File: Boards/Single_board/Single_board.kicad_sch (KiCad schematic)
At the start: 9 parts, among them J1 AUX_I2C_1, J2 AUX_I2C_2, J4 ICSP, Q1 SI2306

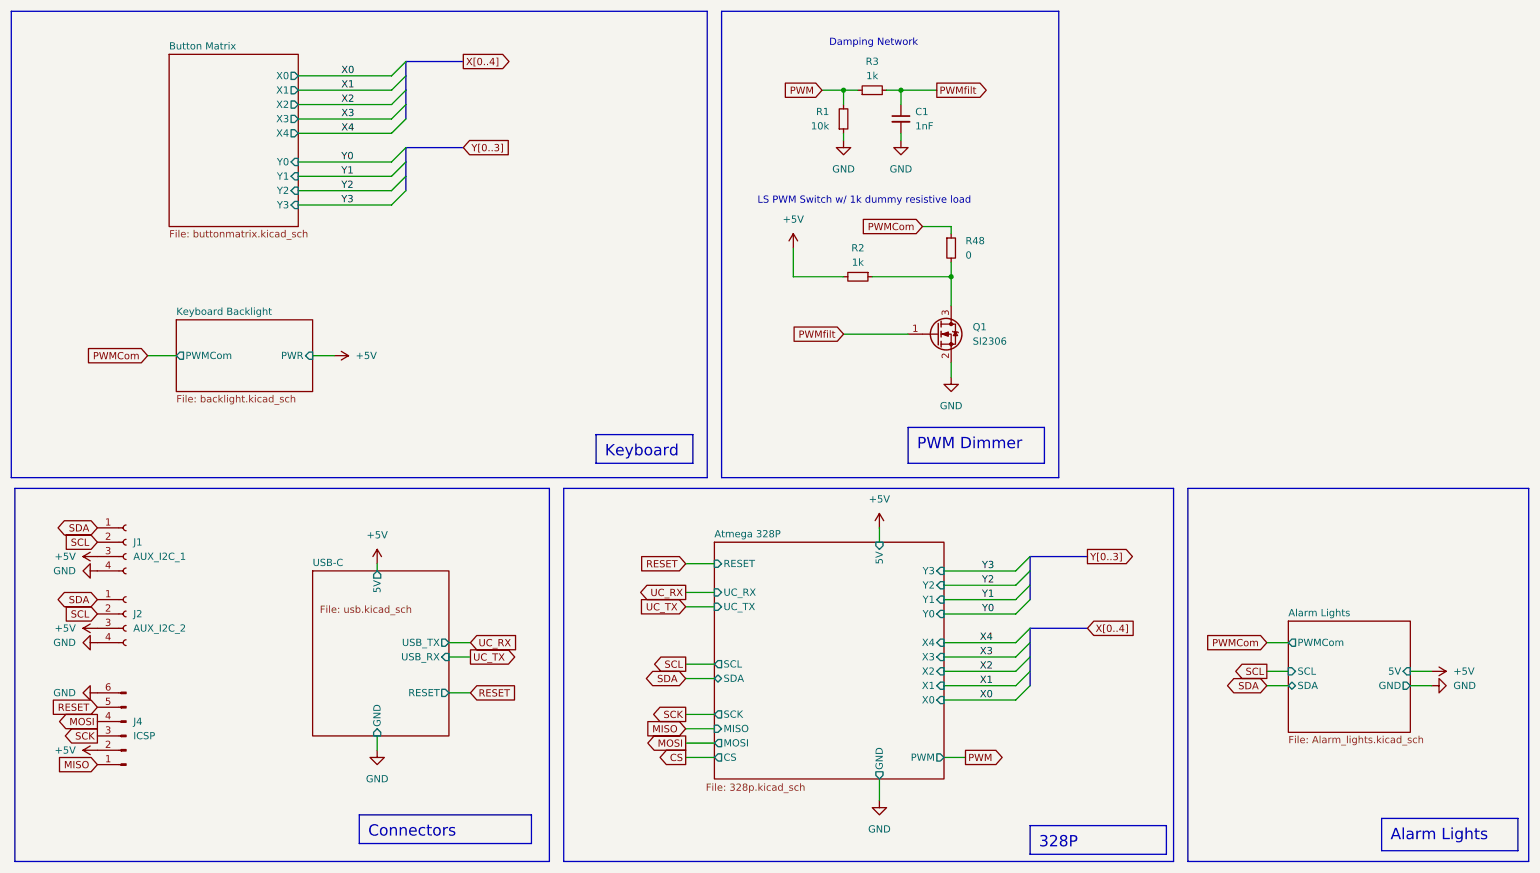
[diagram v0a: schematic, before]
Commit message: Re-stitch and clean up redundant tracks.  Correct some port directions.
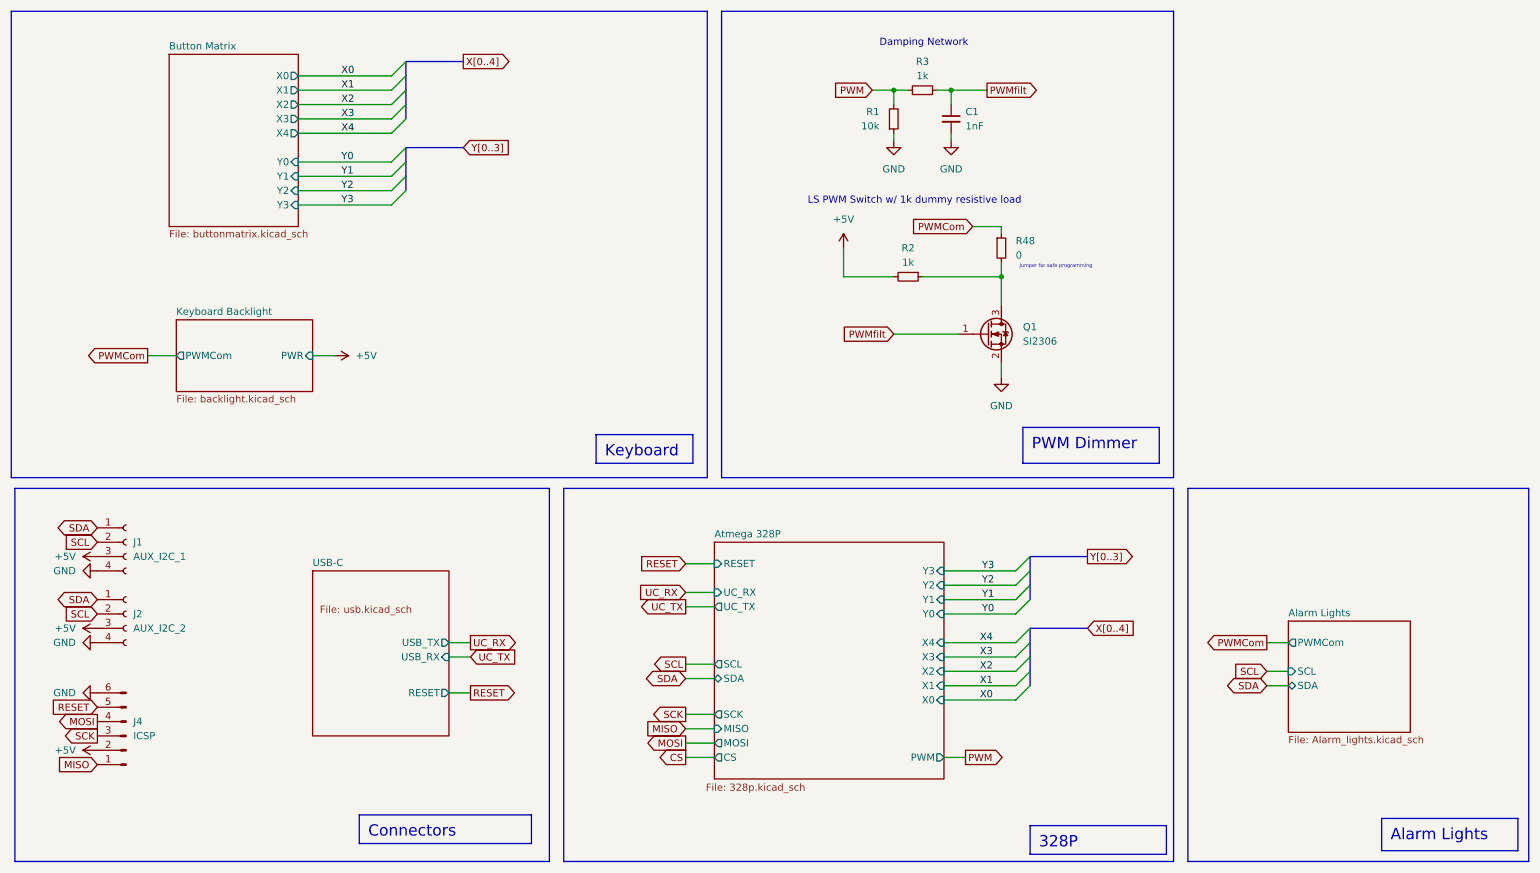
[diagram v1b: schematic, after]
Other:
- sheet Alarm Lights ports: added none; removed 5V, GND
- sheet Atmega 328P ports: added none; removed 5V, GND
- sheet USB-C ports: added none; removed 5V, GND
- note added: "Jumper for safe programming"
- moved on the sheet: C1, Q1, R1, R2, R3, R48

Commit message: Remove redundant GND tracks in place of vias.  Continue rerouting & condensing.  Make PWMCom 20mil
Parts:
- renumbered R48 to SB1
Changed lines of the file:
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@@
 		(dnp no)
 		(fields_autoplaced yes)
-		(property "Reference" "R48"
+		(property "Reference" "SB1"
 			(at 191.77 54.6099 0)
 			(effects
@@
 			(project "Single_board"
 				(path "/f30854c1-5bc2-470d-aabe-1768a5b01b46"
-					(reference "R48")
+					(reference "SB1")
 					(unit 1)
 				)

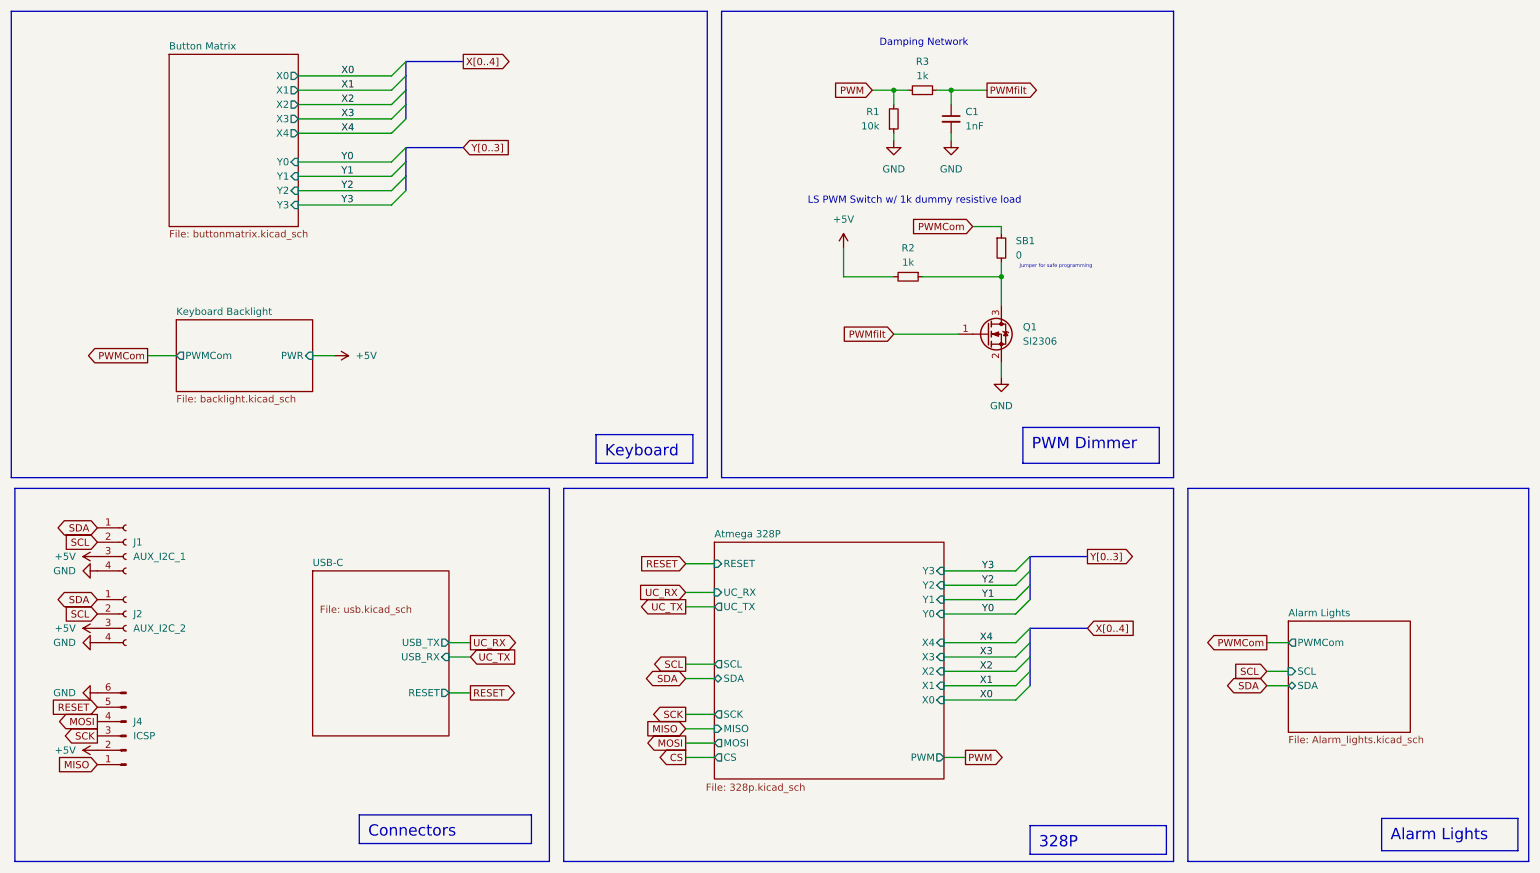
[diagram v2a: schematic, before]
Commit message: Start RGB LED + hotswap socket redesign of single board
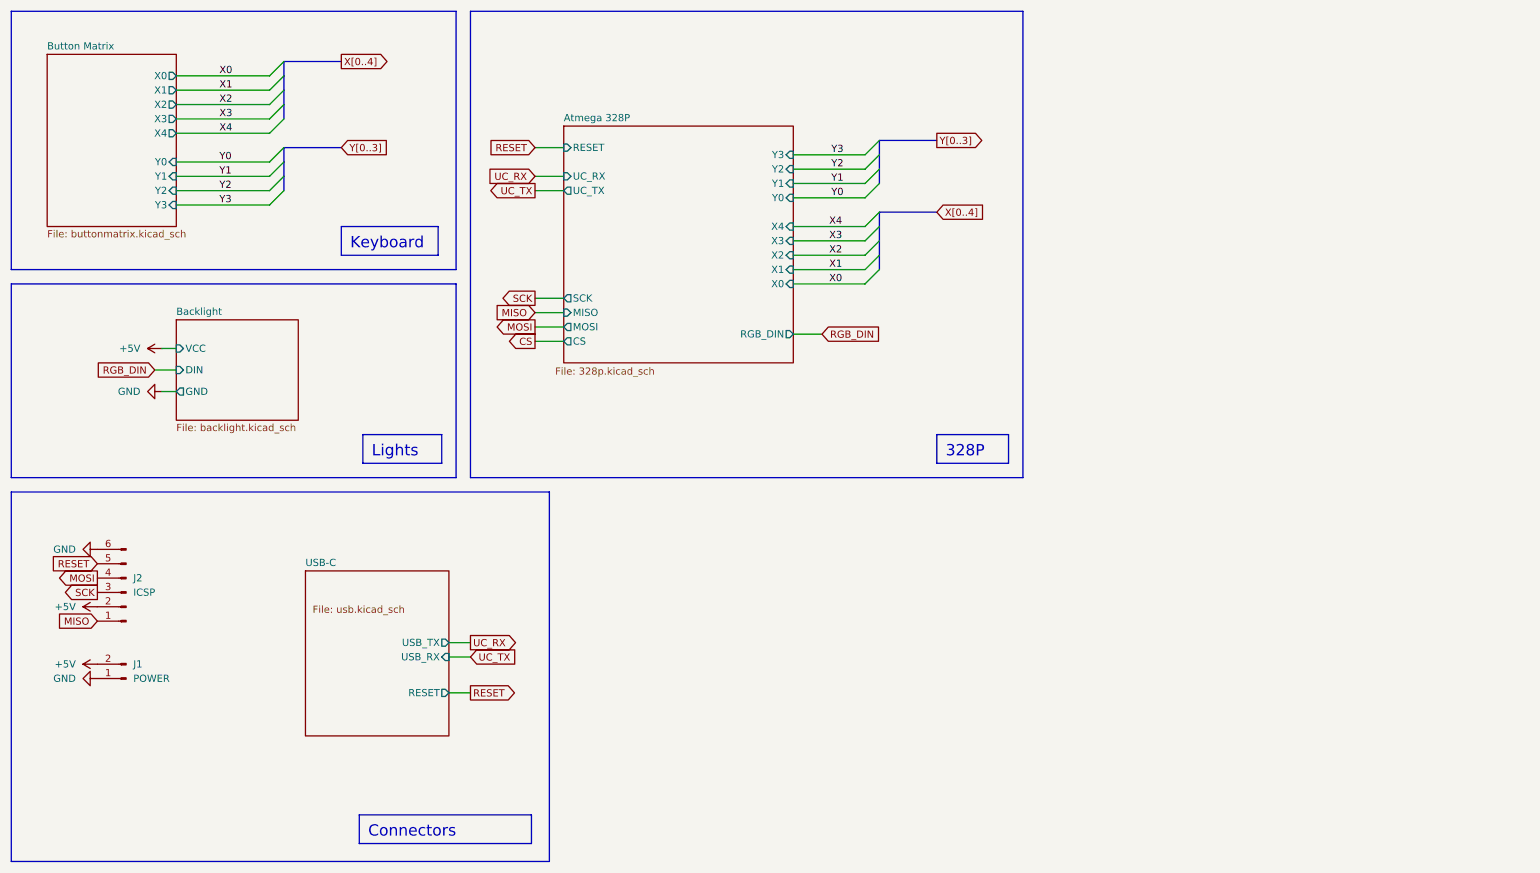
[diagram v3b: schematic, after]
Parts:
- removed C1: 1nF, Capacitor_SMD:C_0805_2012Metric, symbol Device:C_Small
- removed J1: AUX_I2C_1, Connector_JST:JST_XH_B4B-XH-A_1x04_P2.50mm_Vertical, symbol Connector:Conn_01x04_Socket
- removed J2: AUX_I2C_2, Connector_JST:JST_XH_B4B-XH-A_1x04_P2.50mm_Vertical, symbol Connector:Conn_01x04_Socket
- removed Q1: SI2306, Package_TO_SOT_SMD:SOT-23, symbol Device:Q_NMOS_GSD
- removed R1: 10k, Resistor_SMD:R_1206_3216Metric, symbol Device:R_Small
- removed R2, R3: 1k, Resistor_SMD:R_1206_3216Metric, symbol Device:R_Small
- removed SB1: 0, Jumper:SolderJumper-2_P1.3mm_Open_RoundedPad1.0x1.5mm, symbol Device:R_Small
- added J1: POWER, TerminalBlock:TerminalBlock_bornier-2_P5.08mm, symbol Connector:Conn_01x02_Pin
- J2: renamed from J4; footprint Connector_PinHeader_2.54mm:PinHeader_2x03_P2.54mm_Vertical_SMD -> Connector_PinHeader_2.54mm:PinHeader_2x03_P2.54mm_Horizontal
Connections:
- net +5V: now also J1.2 (Pin_2)
- net GND: now also J1.1 (Pin_1)
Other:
- sheet Keyboard Backlight renamed Backlight
- removed sheet Alarm Lights
- sheet Atmega 328P ports: added RGB_DIN; removed PWM, SCL, SDA
- sheet Backlight ports: added DIN, GND, VCC; removed PWMCom, PWR
- note removed: "Damping Network"
- note removed: "Jumper for safe programming"
- note removed: "LS PWM Switch w/ 1k dummy resistive load"
- moved on the sheet: J2

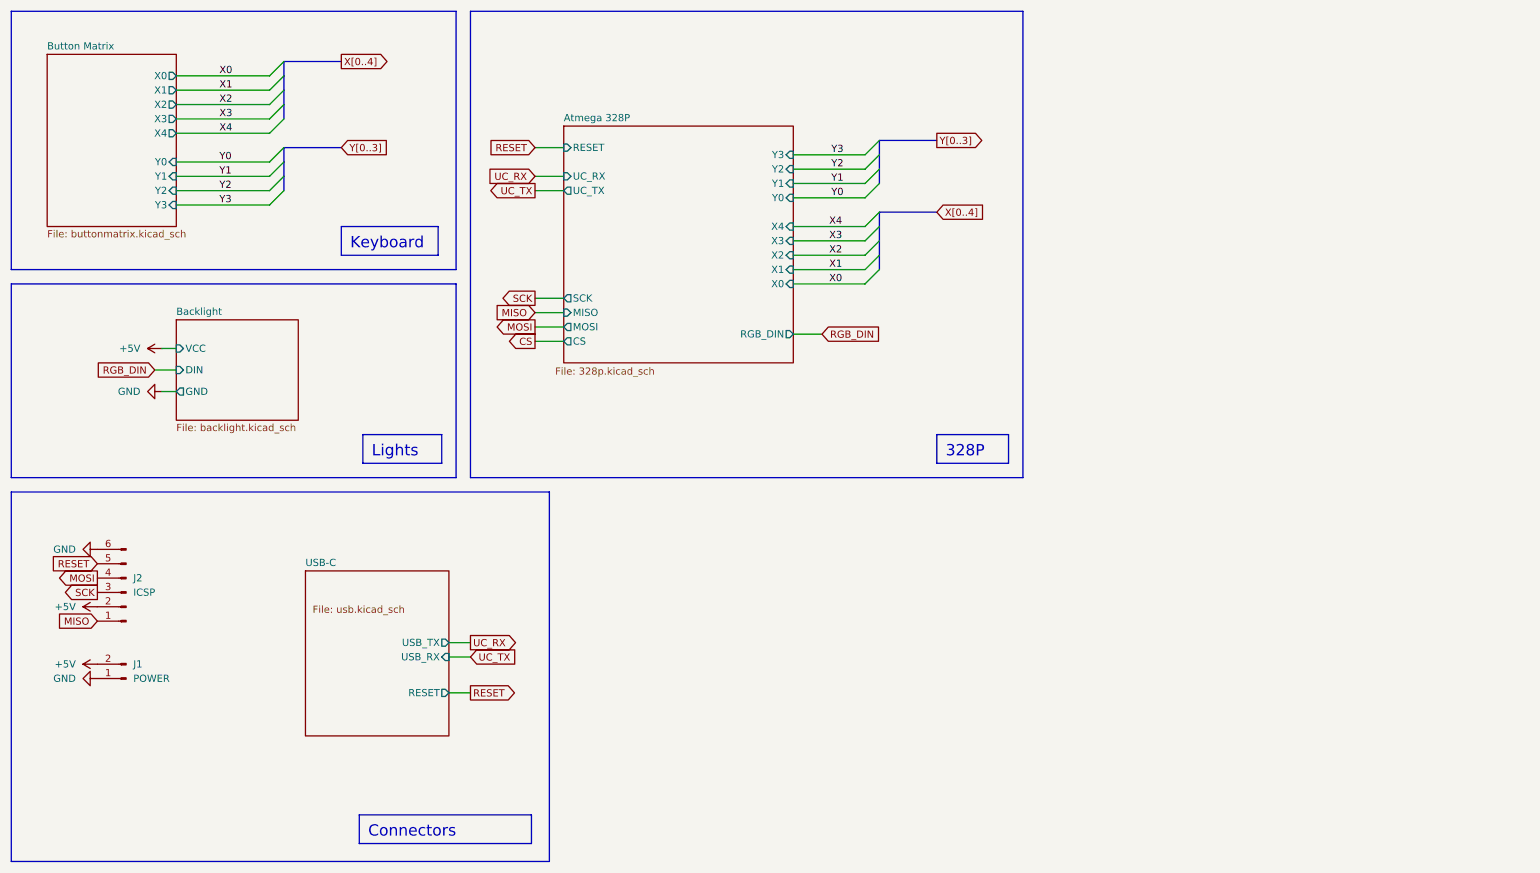
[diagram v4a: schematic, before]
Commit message: Add usb ports and separate power sources. Pending fitting test.
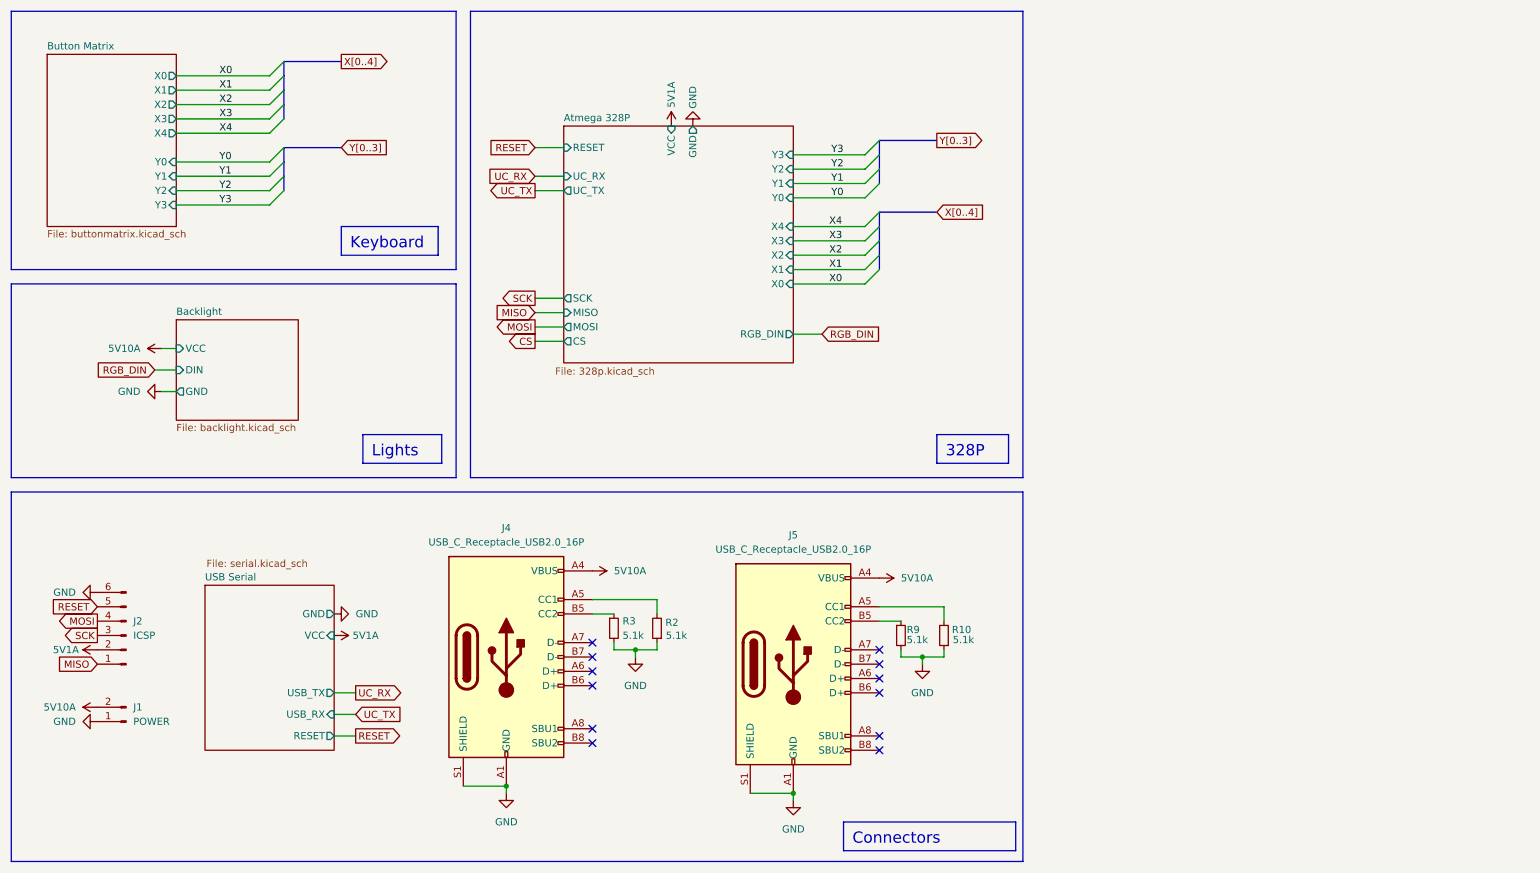
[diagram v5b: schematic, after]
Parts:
- added J4, J5: USB_C_Receptacle_USB2.0_16P, Project Libraries:USB-C-TH_918-468K2029E50001, symbol Connector:USB_C_Receptacle_USB2.0_16P
- added R10, R2, R3, R9: 5.1k, Resistor_SMD:R_0603_1608Metric, symbol Device:R_Small
- J2: footprint Connector_PinHeader_2.54mm:PinHeader_2x03_P2.54mm_Horizontal -> Connector_PinHeader_2.54mm:PinHeader_2x03_P2.54mm_Vertical_SMD
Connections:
- net GND: now also J4.A1 (GND), J4.A12 (GND), J4.B1 (GND), J4.B12 (GND), J4.S1 (SHIELD), J5.A1 (GND), J5.A12 (GND), J5.B1 (GND), J5.B12 (GND), J5.S1 (SHIELD), R10.1, R2.1, R3.2, R9.2
- net +5V renamed 5V10A
- net 5V10A: now also J4.A4 (VBUS), J4.A9 (VBUS), J4.B4 (VBUS), J4.B9 (VBUS), J5.A4 (VBUS), J5.A9 (VBUS), J5.B4 (VBUS), J5.B9 (VBUS); no longer J2.2 (Pin_2)
- new net: J5.B5 (CC2), R9.1
- new net: J5.A5 (CC1), R10.2
- new net: J4.B5 (CC2), R3.1
- new net: J4.A5 (CC1), R2.2
- new net 5V1A: J2.2 (Pin_2)
- no-connect marks 0 -> 12
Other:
- sheet USB-C renamed USB Serial
- sheet Atmega 328P ports: added GND, VCC; removed none
- sheet USB Serial: file usb.kicad_sch -> serial.kicad_sch
- sheet USB Serial ports: added GND, VCC; removed none
- moved on the sheet: J1, J2

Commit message: Board and 3d models update
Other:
- sheet Button Matrix ports: added VCC; removed none
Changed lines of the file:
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@@
 		)
 	)
+	(wire
+		(pts
+			(xy 36.83 20.32) (xy 36.83 21.59)
+		)
+		(stroke
+			(width 0)
+			(type default)
+		)
+	)
 	(bus
 		(pts
@@
 	)
 	(symbol
+		(lib_id "power:+5V")
+		(at 36.83 20.32 0)
+		(unit 1)
+		(exclude_from_sim no)
+		(in_bom yes)
+		(on_board yes)
+		(dnp no)
+		(property "Reference" "#PWR015"
+			(at 36.83 24.13 0)
+			(effects
+				(font
+					(size 1.27 1.27)
+				)
+				(hide yes)
+			)
+		)
+		(property "Value" "5V1A"
+			(at 39.116 16.002 0)
+			(effects
+				(font
+					(size 1.27 1.27)
+				)
+				(justify right)
+			)
+		)
+		(property "Footprint" ""
+			(at 36.83 20.32 0)
+			(effects
+				(font
+					(size 1.27 1.27)
+				)
+				(hide yes)
+			)
+		)
+		(property "Datasheet" ""
+			(at 36.83 20.32 0)
+			(effects
+				(font
+					(size 1.27 1.27)
+				)
+				(hide yes)
+			)
+		)
+		(property "Description" ""
+			(at 36.83 20.32 0)
+			(effects
+				(font
+					(size 1.27 1.27)
+				)
+				(hide yes)
+			)
+		)
+		(pin "1"
+		)
+		(instances
+			(project "Single_board"
+				(path "/f30854c1-5bc2-470d-aabe-1768a5b01b46"
+					(reference "#PWR015")
+					(unit 1)
+				)
+			)
+		)
+	)
+	(symbol
 		(lib_id "power:GND")
 		(at 29.21 139.7 270)
@@
 			(effects
 				(font
+					(size 1.27 1.27)
+				)
+				(justify right)
+			)
+		)
+		(pin "VCC" input
+			(at 36.83 21.59 90)
+			(effects
+				(font
